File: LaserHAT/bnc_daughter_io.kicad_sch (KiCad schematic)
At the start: 11 parts, among them J6 BNC TRIGGER IN, J7 BNC STIM OUT, J8 DB_POWER_TIMING, J9 DB_ANALOG, U8 74LVC2G17

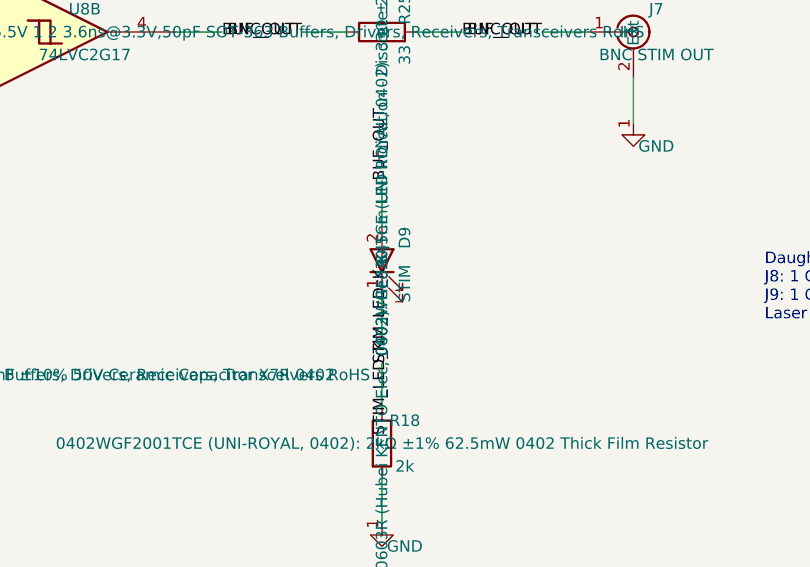
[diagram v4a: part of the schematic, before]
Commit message: LaserHAT: SW8 BACK -> Panasonic EVQP7A01P side-actuated SMD (C79167); Values = part numbers; stamp clears flags
- SW8: schematic footprint Button_Switch_SMD:SW_SPST_EVQP7A; board footprint swapped at the south
  edge (111.55, 98.25), body flush with the edge, button ~0.35 mm proud; BUTTON1 via at the old
  THT pin joins the hand-routed B.Cu run, pad-1 pair bridged; GND pads on the pour. DRC identical
  to before the swap, 0 unconnected; backup stash/LaserDriver_user_2026-09-30_pre-sw8smd.kicad_pcb
- stamp_lcsc.py now also clears DNP / exclude flags on machine-placed parts (SW8 had stayed
  excluded after the previous commit, which wrongly claimed 43 placements)
- Values of LEDs and switches are the part numbers (KT-0603R/W, TS-1088-AR02016, MSK12C02,
  BL-DT, EVQP7A01P, PCM12SMTR) so JLC's BOM matcher sees one part per line; the function names
  remain as silkscreen texts
- verified: lcsc_verify 0 mismatches, sync_check 0 differences (HAT, laser), toolkit BOM/CPL
  consistent in both DNP modes (HAT 29 lines / 43 placements); fab outputs regenerated; docs

Co-Authored-By: Claude Fable 5.1 <noreply@anthropic.com>
Claude-Session: https://claude.ai/code/session_018vgLizGzYPynnY93ajvoVA
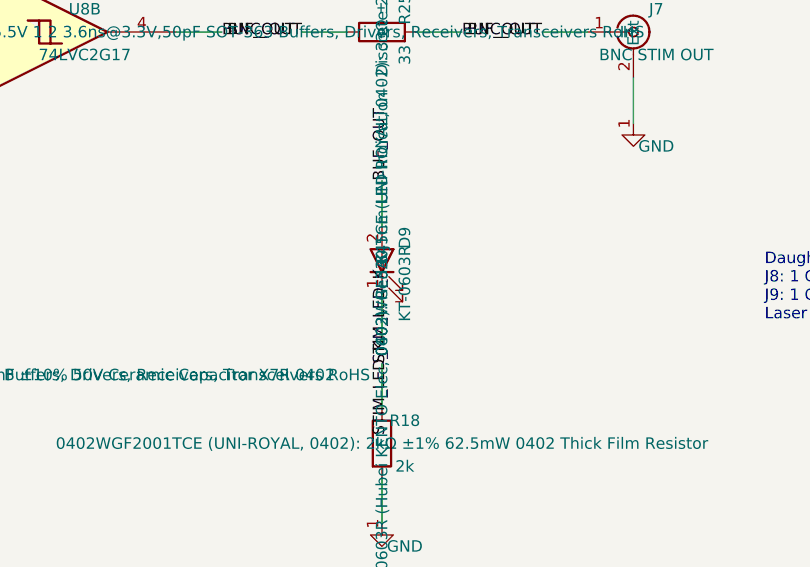
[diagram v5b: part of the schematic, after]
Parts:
- D9: value STIM -> KT-0603R
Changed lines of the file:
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@@
 			)
 		)
-		(property "Value" "STIM"
+		(property "Value" "KT-0603R"
 			(at 160.02 129.54 0)
 			(effects
